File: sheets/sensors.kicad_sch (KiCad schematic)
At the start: 13 parts, among them CN1 StemmaQT, U2 BMP581, U3 SparkfunM9N, U5 ADXL375BCCZ-RL7, U7 ADXL345BCCZ-RL7

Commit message: second push
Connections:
- net VCC is gone; now on net +3V3: CN1.2
- net +3V3: now also CIO1.1, CIO2.1, CS1.1, U5.1 (VDDI/O), U5.6 (VS), U7.1 (VDD_I/O)
- net VDD: no longer CIO1.1, CIO2.1, CS1.1, U5.1 (VDDI/O), U5.6 (VS), U7.1 (VDD_I/O)

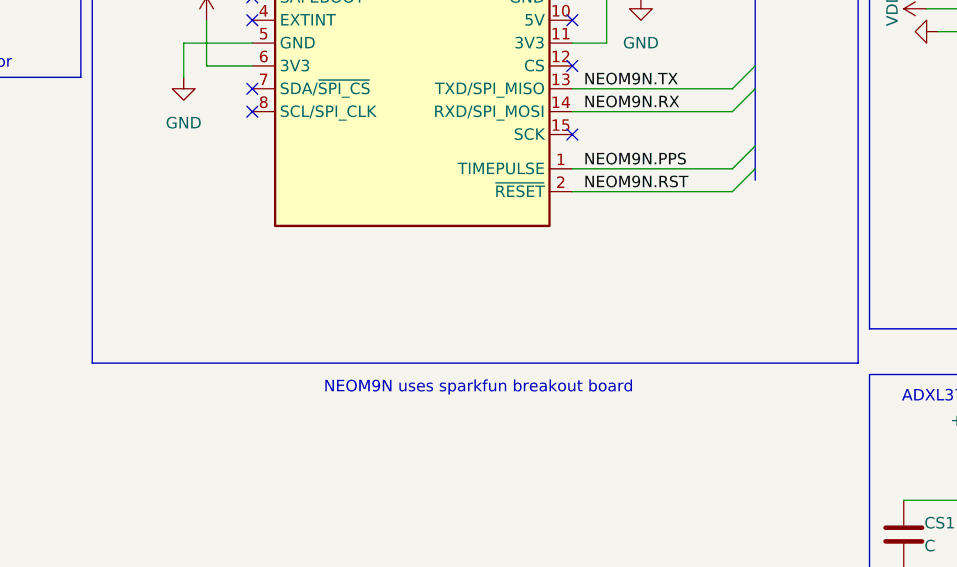
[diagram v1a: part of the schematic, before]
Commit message: removed fd can
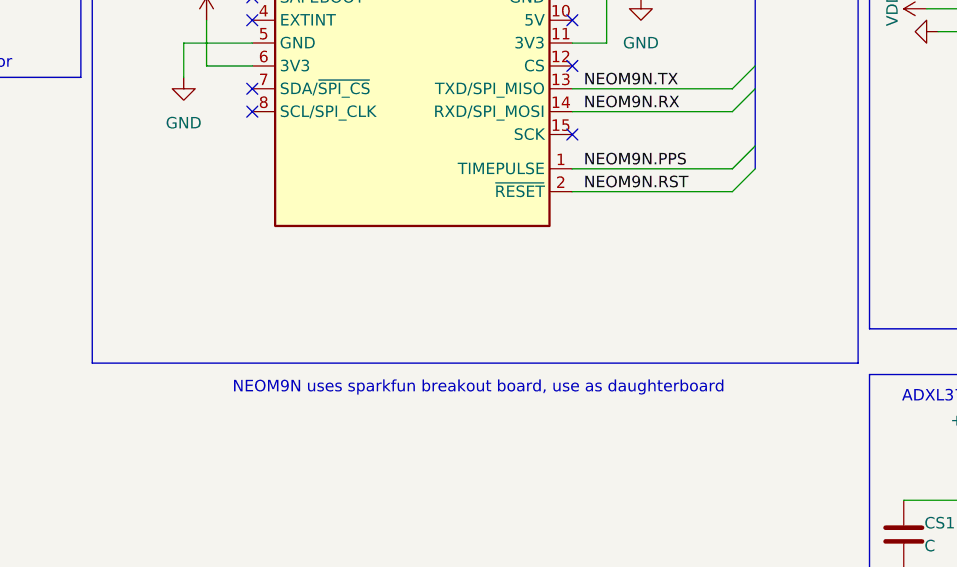
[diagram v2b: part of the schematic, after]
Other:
- note added: "NEOM9N uses sparkfun breakout board, use as daughterboard"
- note removed: "NEOM9N uses sparkfun breakout board"
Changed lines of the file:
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@@
 		)
 	)
-	(text "NEOM9N uses sparkfun breakout board"
+	(text "NEOM9N uses sparkfun breakout board, use as daughterboard"
 		(exclude_from_sim no)
 		(at 122.936 95.504 0)
@@
 		)
 		(stroke
-			(width 0)
-			(type default)
-		)
-	)
-	(bus
-		(pts
-			(xy 153.67 71.12) (xy 153.67 72.39)
-		)
-		(stroke

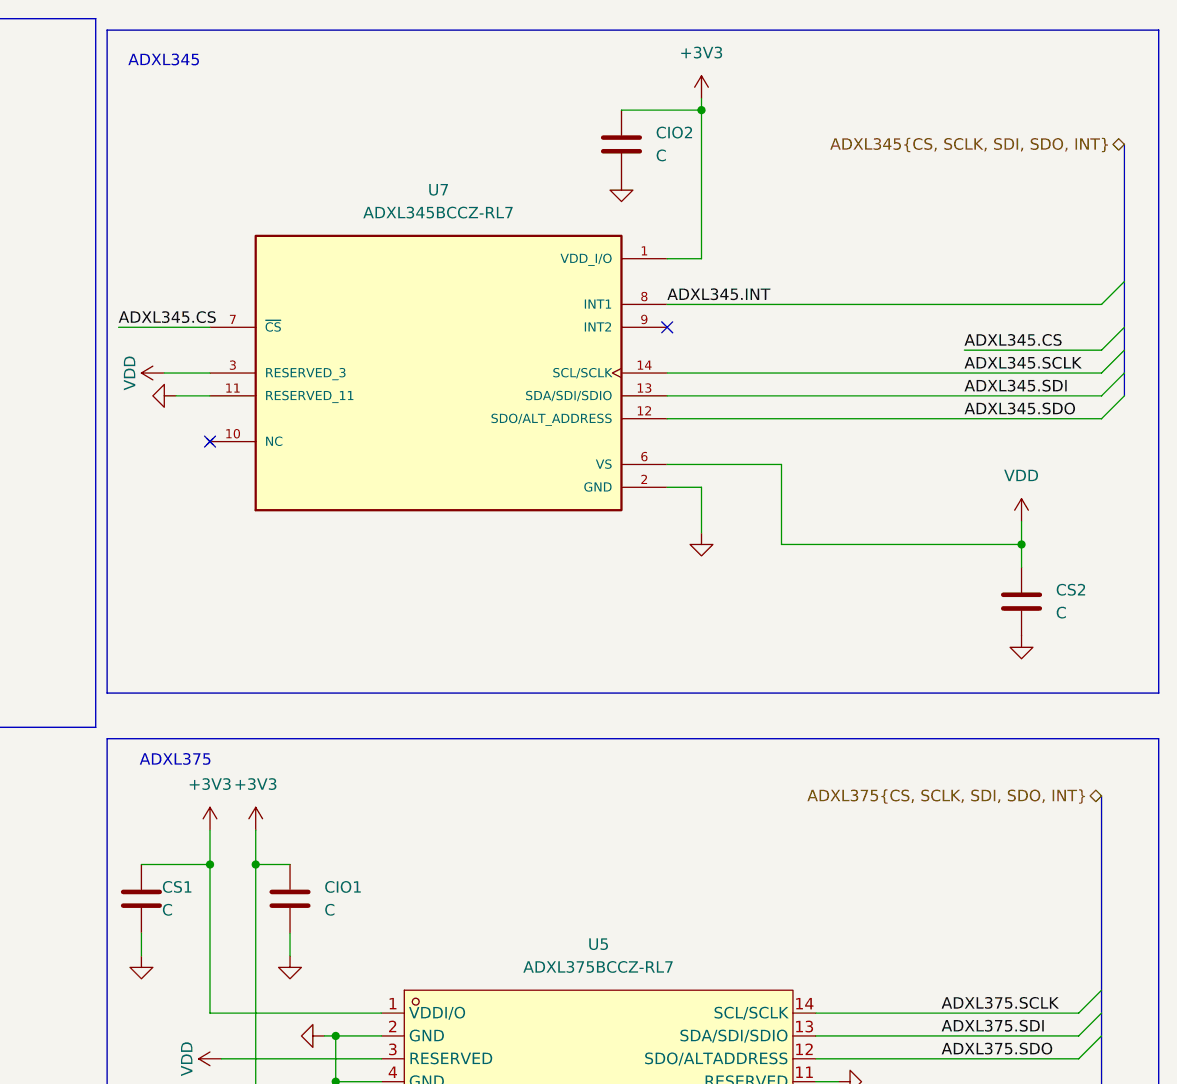
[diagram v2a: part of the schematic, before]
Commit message: added Capacitor values for sensors
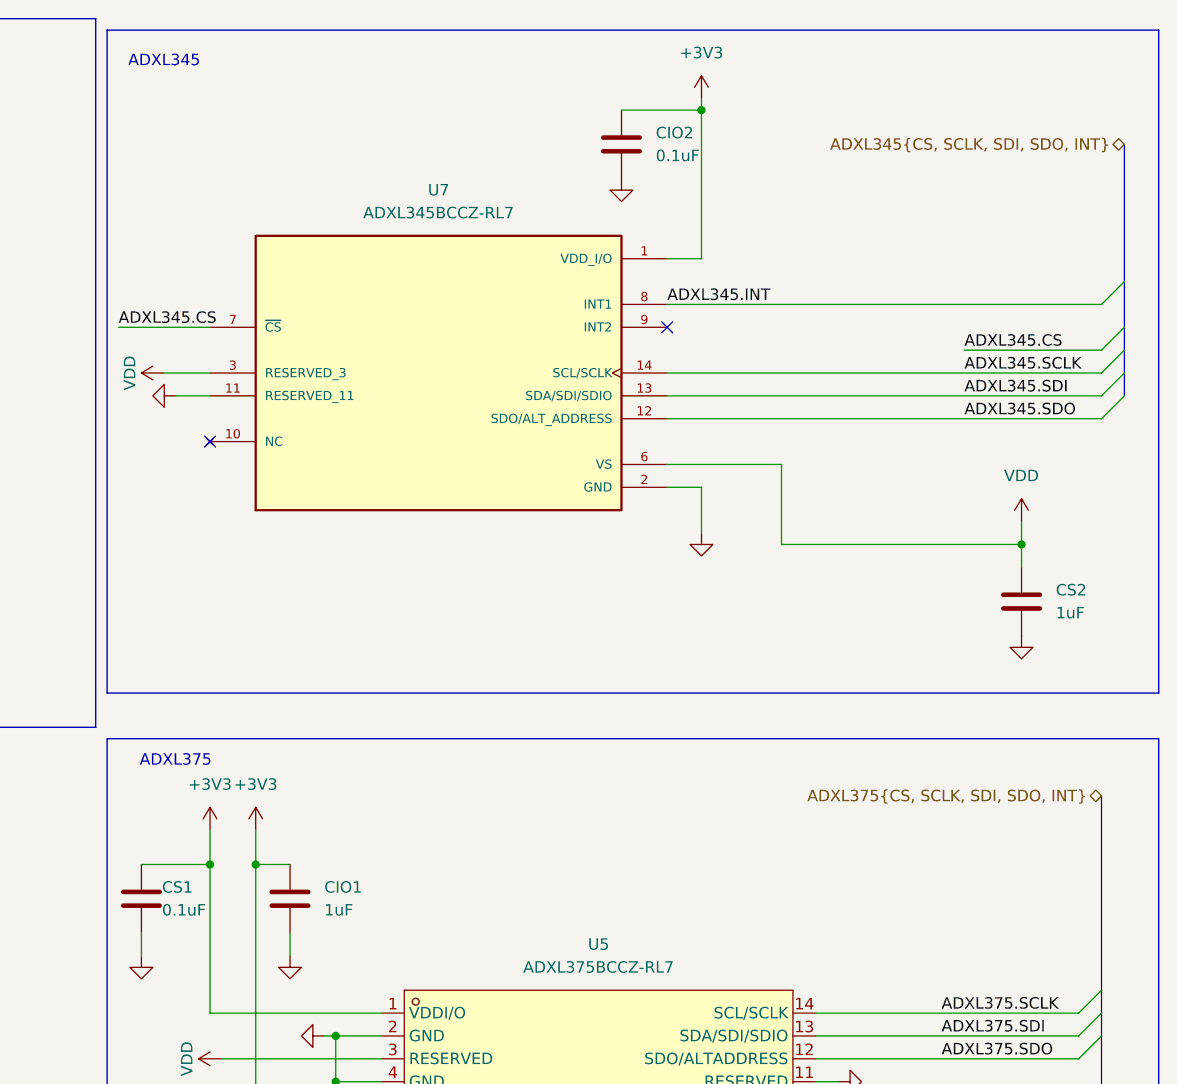
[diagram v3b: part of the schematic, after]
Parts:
- CIO1, CS2: value C -> 1uF
- CIO2, CS1: value C -> 0.1uF
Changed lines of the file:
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@@
 			)
 		)
-		(property "Value" "C"
+		(property "Value" "1uF"
 			(at 271.78 80.0099 0)
 			(effects
@@
 			)
 		)
-		(property "Value" "C"
+		(property "Value" "0.1uF"
 			(at 227.33 29.2099 0)
 			(effects
@@
 			)
 		)
-		(property "Value" "C"
+		(property "Value" "0.1uF"
 			(at 172.466 113.03 0)
 			(effects
@@
 			)
 		)
-		(property "Value" "C"
+		(property "Value" "1uF"
 			(at 190.5 113.0299 0)
 			(effects

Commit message: assigned gpio pin to led (pg6)
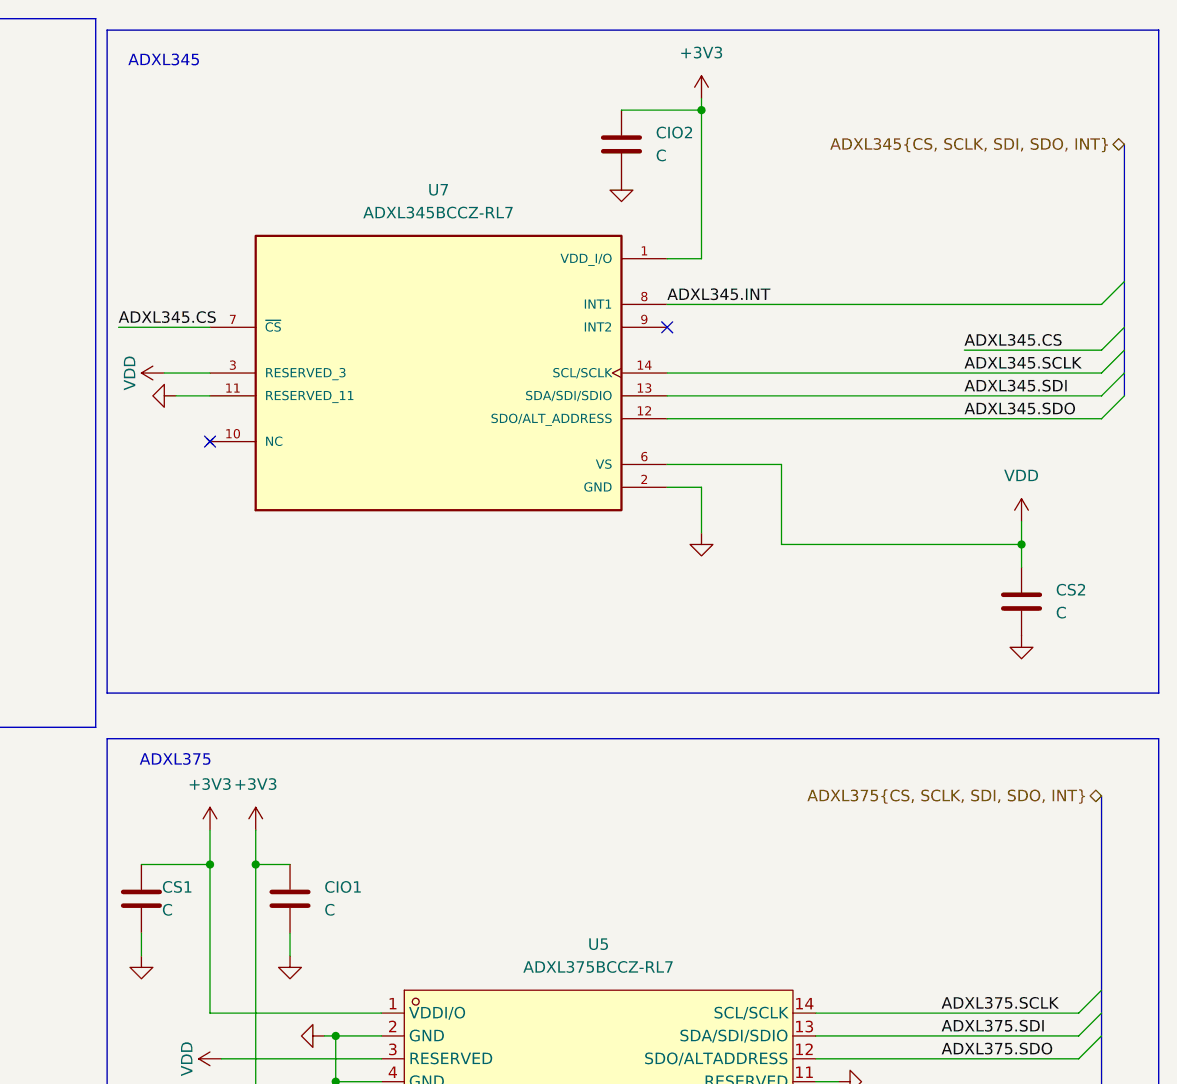
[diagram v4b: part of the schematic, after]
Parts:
- CIO1, CS2: value 1uF -> C
- CIO2, CS1: value 0.1uF -> C
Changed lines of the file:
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@@
 			)
 		)
-		(property "Value" "1uF"
+		(property "Value" "C"
 			(at 271.78 80.0099 0)
 			(effects
@@
 			)
 		)
-		(property "Value" "0.1uF"
+		(property "Value" "C"
 			(at 227.33 29.2099 0)
 			(effects
@@
 			)
 		)
-		(property "Value" "0.1uF"
+		(property "Value" "C"
 			(at 172.466 113.03 0)
 			(effects
@@
 			)
 		)
-		(property "Value" "1uF"
+		(property "Value" "C"
 			(at 190.5 113.0299 0)
 			(effects

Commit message: final rev1
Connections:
- net +3V3: now also R24.1, R25.1
- net VDD: no longer R24.1, R25.1
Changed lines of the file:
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@@
+	)
+	(symbol
+		(lib_id "power:+3V3")
+		(at 33.02 138.43 0)
+		(unit 1)
+		(exclude_from_sim no)
+		(in_bom yes)
+		(on_board yes)
+		(dnp no)
+		(fields_autoplaced yes)
+		(property "Reference" "#PWR048"
+			(at 33.02 142.24 0)
+			(effects
+				(font
+					(size 1.27 1.27)
+				)
+				(hide yes)
+			)
+		)
+		(property "Value" "+3V3"
+			(at 33.02 133.35 0)
+			(effects
+				(font
+					(size 1.27 1.27)
+				)
+			)
+		)
+		(property "Footprint" ""
+			(at 33.02 138.43 0)
+			(effects
+				(font
+					(size 1.27 1.27)
+				)
+				(hide yes)
+			)
+		)
+		(property "Datasheet" ""
+			(at 33.02 138.43 0)
+			(effects
+				(font
+					(size 1.27 1.27)
+				)
+				(hide yes)
+			)
+		)
+		(property "Description" "Power symbol creates a global label with name \"+3V3\""
+			(at 33.02 138.43 0)
+			(effects
+				(font
+					(size 1.27 1.27)
+				)
+				(hide yes)
+			)
+		)
+		(pin "1"
+		)
+		(instances
+			(project "aerolotl"
+				(path "/3f5bc5ea-feaa-4ed9-b0e0-c918b1fb5754/74e9b1e9-3a21-4de4-9795-bce3dd5092b3"
+					(reference "#PWR048")
+					(unit 1)
+				)
+			)
+		)
 	)
 	(symbol
@@
 				(path "/3f5bc5ea-feaa-4ed9-b0e0-c918b1fb5754/74e9b1e9-3a21-4de4-9795-bce3dd5092b3"
 					(reference "#PWR034")
-					(unit 1)
-				)
-			)
-		)
-	)
-	(symbol
-		(lib_id "power:VDD")
-		(at 33.02 138.43 0)
-		(unit 1)
-		(exclude_from_sim no)
-		(in_bom yes)
-		(on_board yes)
-		(dnp no)
-		(fields_autoplaced yes)
-		(property "Reference" "#PWR048"
-			(at 33.02 142.24 0)
-			(effects
-				(font
-					(size 1.27 1.27)
-				)
-				(hide yes)
-			)
-		)
-		(property "Value" "VDD"
-			(at 33.02 133.35 0)
-			(effects
-				(font
-					(size 1.27 1.27)
-				)
-			)
-		)
-		(property "Footprint" ""
-			(at 33.02 138.43 0)
-			(effects
-				(font
-					(size 1.27 1.27)
-				)
-				(hide yes)
-			)
-		)
-		(property "Datasheet" ""
-			(at 33.02 138.43 0)
-			(effects
-				(font
-					(size 1.27 1.27)
-				)
-				(hide yes)
-			)
-		)
-		(property "Description" "Power symbol creates a global label with name \"VDD\""
-			(at 33.02 138.43 0)
-			(effects
-				(font
-					(size 1.27 1.27)
-				)
-				(hide yes)
-			)
-		)
-		(pin "1"
-		)
-		(instances
-			(project "aerolotl"
-				(path "/3f5bc5ea-feaa-4ed9-b0e0-c918b1fb5754/74e9b1e9-3a21-4de4-9795-bce3dd5092b3"
-					(reference "#PWR048")
 					(unit 1)
 				)
@@
 	)
 	(symbol
-		(lib_id "power:VDD")
+		(lib_id "power:+3V3")
+		(at 177.8 104.14 0)
+		(unit 1)
+		(exclude_from_sim no)
+		(in_bom yes)
+		(on_board yes)
+		(dnp no)
+		(fields_autoplaced yes)
+		(property "Reference" "#PWR060"
+			(at 177.8 107.95 0)
+			(effects
+				(font
+					(size 1.27 1.27)
+				)
+				(hide yes)
+			)
+		)
+		(property "Value" "+3V3"
+			(at 177.8 99.06 0)
+			(effects
+				(font
+					(size 1.27 1.27)
+				)
+			)
+		)
+		(property "Footprint" ""
+			(at 177.8 104.14 0)
+			(effects
+				(font
+					(size 1.27 1.27)
+				)
+				(hide yes)
+			)
+		)
+		(property "Datasheet" ""
+			(at 177.8 104.14 0)
+			(effects
+				(font
+					(size 1.27 1.27)
+				)
+				(hide yes)
+			)
+		)
+		(property "Description" "Power symbol creates a global label with name \"+3V3\""
+			(at 177.8 104.14 0)
+			(effects
+				(font
+					(size 1.27 1.27)
+				)
+				(hide yes)
+			)
+		)
+		(pin "1"
+		)
+		(instances
+			(project "aerolotl"
+				(path "/3f5bc5ea-feaa-4ed9-b0e0-c918b1fb5754/74e9b1e9-3a21-4de4-9795-bce3dd5092b3"
+					(reference "#PWR060")
+					(unit 1)
+				)
+			)
+		)
+	)
+	(symbol
+		(lib_id "power:GND")
+		(at 140.97 52.07 0)
+		(unit 1)
+		(exclude_from_sim no)
+		(in_bom yes)
+		(on_board yes)
+		(dnp no)
+		(fields_autoplaced yes)
+		(property "Reference" "#PWR093"
+			(at 140.97 58.42 0)
+			(effects
+				(font
+					(size 1.27 1.27)
+				)
+				(hide yes)
+			)
+		)
+		(property "Value" "GND"
+			(at 140.97 57.15 0)
+			(effects
+				(font
+					(size 1.27 1.27)
+				)
+			)
+		)
+		(property "Footprint" ""
+			(at 140.97 52.07 0)
+			(effects
+				(font
+					(size 1.27 1.27)
+				)
+				(hide yes)
+			)
+		)
+		(property "Datasheet" ""
+			(at 140.97 52.07 0)
+			(effects
+				(font
+					(size 1.27 1.27)
+				)
+				(hide yes)
+			)
+		)
+		(property "Description" "Power symbol creates a global label with name \"GND\" , ground"
+			(at 140.97 52.07 0)
+			(effects
+				(font
+					(size 1.27 1.27)
+				)
+				(hide yes)
+			)
+		)
+		(pin "1"
+		)
+		(instances
+			(project "aerolotl"
+				(path "/3f5bc5ea-feaa-4ed9-b0e0-c918b1fb5754/74e9b1e9-3a21-4de4-9795-bce3dd5092b3"
+					(reference "#PWR093")
+					(unit 1)
+				)
+			)
+		)
+	)
+	(symbol
+		(lib_id "power:+3V3")
 		(at 73.66 138.43 0)
 		(unit 1)
@@
 			)
 		)
-		(property "Value" "VDD"
+		(property "Value" "+3V3"
 			(at 73.66 133.35 0)
 			(effects
@@
 			)
 		)
-		(property "Description" "Power symbol creates a global label with name \"VDD\""
+		(property "Description" "Power symbol creates a global label with name \"+3V3\""
 			(at 73.66 138.43 0)
 			(effects
@@
 					(unit 1)
 				)
-			)
-		)
-	)
-	(symbol
-		(lib_id "power:+3V3")
-		(at 177.8 104.14 0)
-		(unit 1)
-		(exclude_from_sim no)
-		(in_bom yes)
-		(on_board yes)
-		(dnp no)
-		(fields_autoplaced yes)
-		(property "Reference" "#PWR060"
-			(at 177.8 107.95 0)
-			(effects
-				(font
-					(size 1.27 1.27)
-				)
-				(hide yes)
-			)
-		)
-		(property "Value" "+3V3"
-			(at 177.8 99.06 0)
-			(effects
-				(font
-					(size 1.27 1.27)
-				)
-			)
-		)
-		(property "Footprint" ""
-			(at 177.8 104.14 0)
-			(effects
-				(font
-					(size 1.27 1.27)
-				)
-				(hide yes)
-			)
-		)
-		(property "Datasheet" ""
-			(at 177.8 104.14 0)
-			(effects
-				(font
-					(size 1.27 1.27)
-				)
-				(hide yes)
-			)
-		)
-		(property "Description" "Power symbol creates a global label with name \"+3V3\""
-			(at 177.8 104.14 0)
-			(effects
-				(font
-					(size 1.27 1.27)
-				)
-				(hide yes)
-			)
-		)
-		(pin "1"
-		)
-		(instances
-			(project "aerolotl"
-				(path "/3f5bc5ea-feaa-4ed9-b0e0-c918b1fb5754/74e9b1e9-3a21-4de4-9795-bce3dd5092b3"
-					(reference "#PWR060")
-					(unit 1)
-				)
-			)
-		)
-	)
-	(symbol
-		(lib_id "power:GND")
-		(at 140.97 52.07 0)
-		(unit 1)
-		(exclude_from_sim no)
-		(in_bom yes)
-		(on_board yes)
-		(dnp no)
-		(fields_autoplaced yes)
-		(property "Reference" "#PWR093"
-			(at 140.97 58.42 0)
-			(effects
-				(font
-					(size 1.27 1.27)
-				)
-				(hide yes)
-			)
-		)
-		(property "Value" "GND"
-			(at 140.97 57.15 0)
-			(effects
-				(font
-					(size 1.27 1.27)
-				)
-			)
-		)
-		(property "Footprint" ""
-			(at 140.97 52.07 0)
-			(effects
-				(font
-					(size 1.27 1.27)
-				)
-				(hide yes)
-			)
-		)
-		(property "Datasheet" ""
-			(at 140.97 52.07 0)
-			(effects
-				(font
-					(size 1.27 1.27)
-				)
-				(hide yes)
-			)
-		)
-		(property "Description" "Power symbol creates a global label with name \"GND\" , ground"
-			(at 140.97 52.07 0)
-			(effects
-				(font
-					(size 1.27 1.27)
-				)
-				(hide yes)
-			)
-		)
-		(pin "1"
-		)
-		(instances
-			(project "aerolotl"
-				(path "/3f5bc5ea-feaa-4ed9-b0e0-c918b1fb5754/74e9b1e9-3a21-4de4-9795-bce3dd5092b3"
-					(reference "#PWR093")
-					(unit 1)
-				)

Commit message: Rev1 schematic done
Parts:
- U9: renamed from U5; footprint aerolotl_custom:LGA-14_L5.0-W3.0-P0.80-BL -> aerolotl_custom:ADXL375_LGA-14_L5.0-W3.0-P0.80-BL
- renumbered C32 to C42, C33 to C43, R24 to R17, R25 to R18, U3 to U6, U2 to U7, U7 to U8
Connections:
- net VDD is gone; now on net +3V3: CS2.1, U8.3 (RESERVED_3), U8.6 (VS), U9.3 (RESERVED)
